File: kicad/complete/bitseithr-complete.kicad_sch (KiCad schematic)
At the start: 60 parts, among them CN1 SHIELD CONN 2, CN10 SHIELD CONN 3, CN11 SHIELD CONN 4, CN12 SHIELD CONN 5, CN2 SHIELD CONN 7, CN3 SHIELD CONN 8, CN4 PIGTAIL 4, CN5 PIGTAIL 3, CN6 PIGTAIL 5, CN7 PIGTAIL 1, CN8 PIGTAIL 2, CN9 SHIELD CONN 6, IC1 AY-3-8912_28PIN, IC2 AY-3-8912_28PIN, J1 lil-joystick, J10 Communication, J11 OLED Connector, J2 AUDIO JACK 1, J3 AUDIO JACK 2, J4 Power, J5 Analog, J6 Analog, J7 Digital, J8 PWM, J9 PWM, P1 SHIELD CONN 1, SW1 POWER SWITCH, U1 OPA1692

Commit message: idk why i had to save again but this should be it for v1 of the schematic
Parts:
- renumbered C8 to C10, C9 to C11, C10 to C12, C11 to C13, C12 to C14, C13 to C15, C14 to C7, C15 to C8, C7 to C9

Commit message: continued work on keyboard pcb
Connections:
- net OUTPUT-1: no longer CN11.1
- net OUTPUT-2: now also CN11.1
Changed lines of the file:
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@@
 		)
 	)
-	(global_label "OUTPUT-1"
+	(global_label "OUTPUT-2"
 		(shape input)
 		(at 173.99 137.16 180)

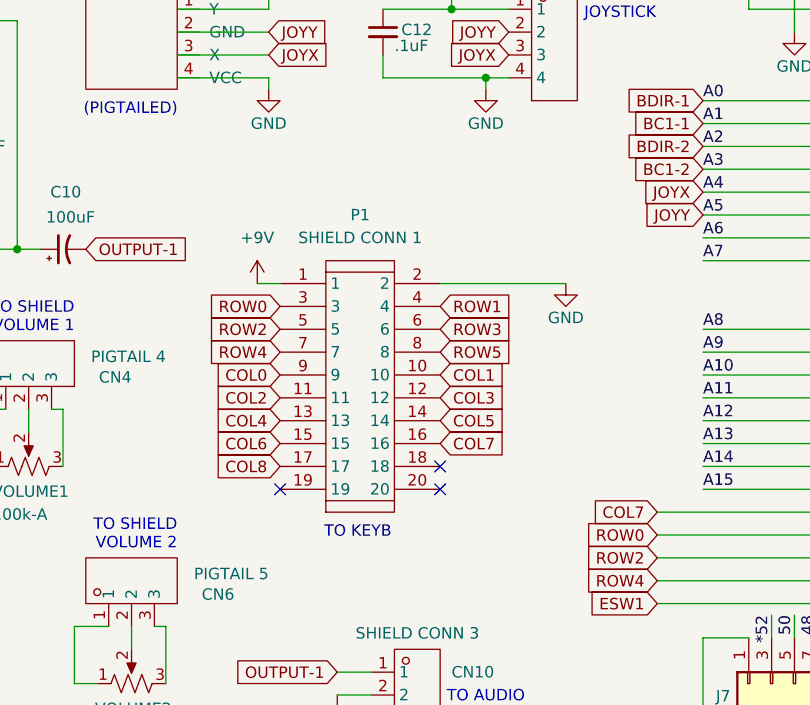
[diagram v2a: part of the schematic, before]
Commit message: updated keyboard connector pinout for better trace routing (hopefully)
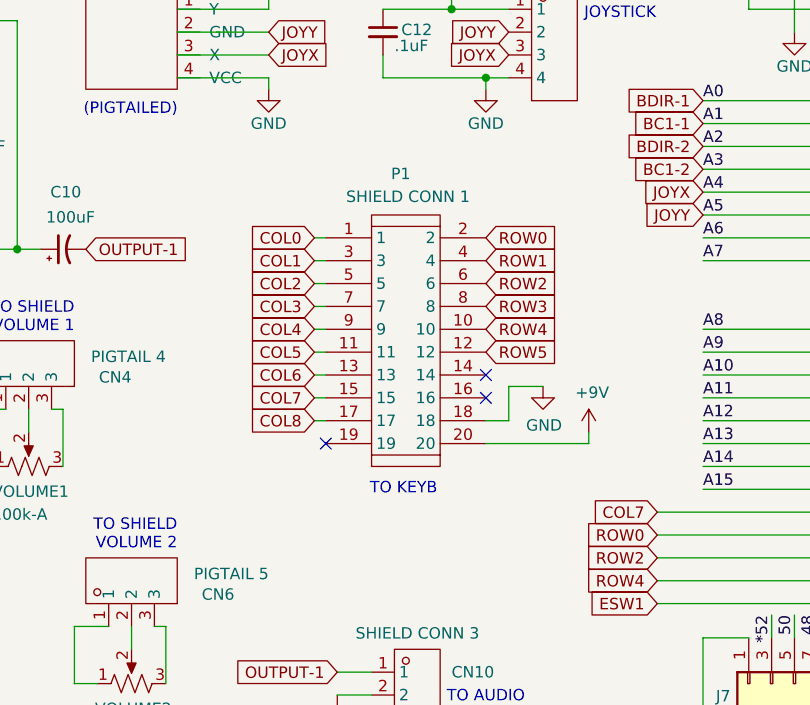
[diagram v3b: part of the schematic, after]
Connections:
- net +9V: now also P1.20; no longer P1.1
- net COL0: now also P1.1; no longer P1.9
- net COL1: now also P1.3; no longer P1.10
- net COL2: now also P1.5; no longer P1.11
- net COL3: now also P1.7; no longer P1.12
- net COL4: now also P1.9; no longer P1.13
- net COL5: now also P1.11; no longer P1.14
- net COL6: now also P1.13; no longer P1.15
- net COL7: now also P1.15; no longer P1.16
- net GND: now also P1.18; no longer P1.2
- net ROW0: now also P1.2; no longer P1.3
- net ROW2: now also P1.6; no longer P1.5
- net ROW3: now also P1.8; no longer P1.6
- net ROW4: now also P1.10; no longer P1.7
- net ROW5: now also P1.12; no longer P1.8

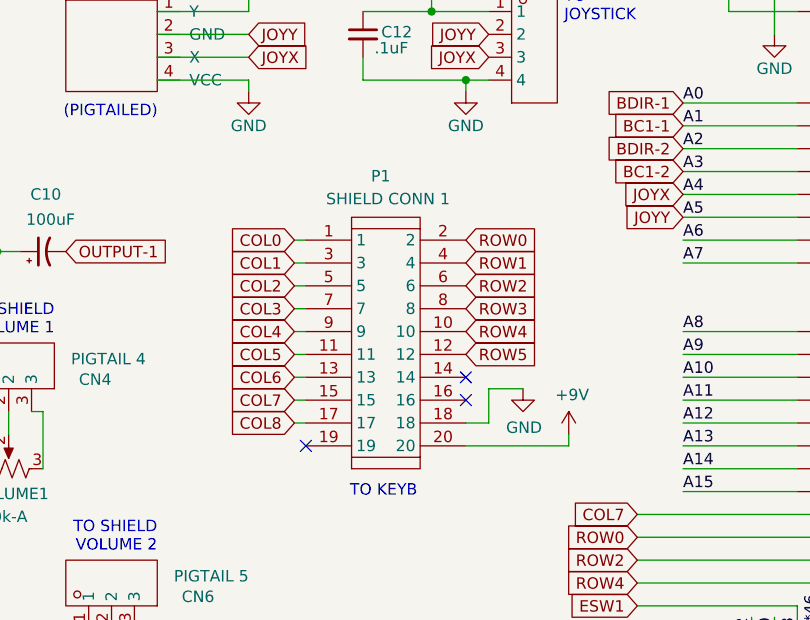
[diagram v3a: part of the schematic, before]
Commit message: updated keyboard connector pinout again for better routing
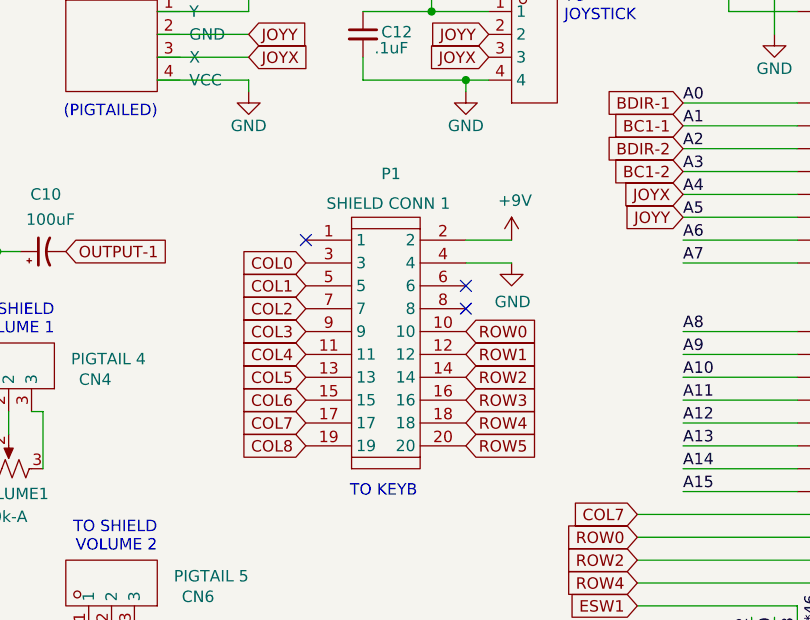
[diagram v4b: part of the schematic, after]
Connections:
- net +9V: now also P1.2; no longer P1.20
- net COL0: now also P1.3; no longer P1.1
- net COL1: now also P1.5; no longer P1.3
- net COL2: now also P1.7; no longer P1.5
- net COL3: now also P1.9; no longer P1.7
- net COL4: now also P1.11; no longer P1.9
- net COL5: now also P1.13; no longer P1.11
- net COL6: now also P1.15; no longer P1.13
- net COL7: now also P1.17; no longer P1.15
- net COL8: now also P1.19; no longer P1.17
- net GND: now also P1.4; no longer P1.18
- net ROW0: now also P1.10; no longer P1.2
- net ROW1: now also P1.12; no longer P1.4
- net ROW2: now also P1.14; no longer P1.6
- net ROW3: now also P1.16; no longer P1.8
- net ROW4: now also P1.18; no longer P1.10
- net ROW5: now also P1.20; no longer P1.12
